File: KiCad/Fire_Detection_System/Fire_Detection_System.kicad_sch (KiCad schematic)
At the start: 12 parts, among them J1 Conn_01x19_Female, J10 Conn_01x01_Pin, J2 Conn_01x19_Female, J3 Conn_01x01_Pin, J4 Conn_01x01_Pin, J5 Conn_01x01_Pin, J6 Conn_01x01_Pin, J7 Conn_01x01_Pin, J8 Conn_01x01_Pin, J9 Conn_01x01_Pin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

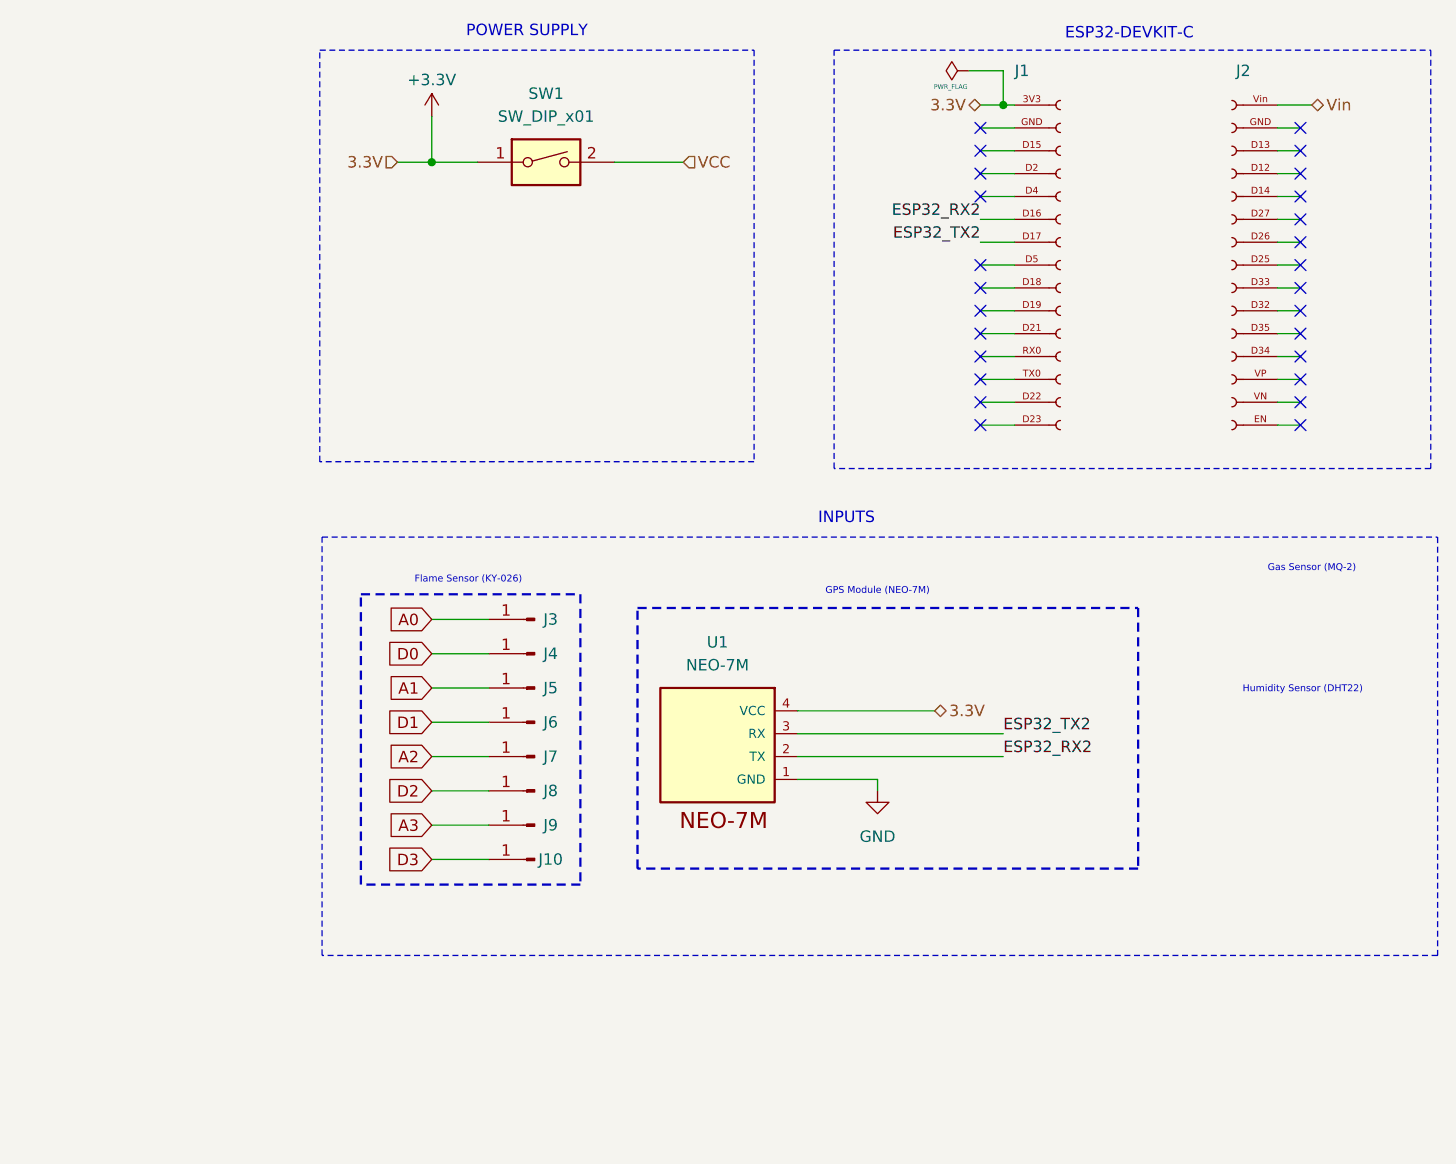
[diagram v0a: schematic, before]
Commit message: feat: Adding Compass Calibration
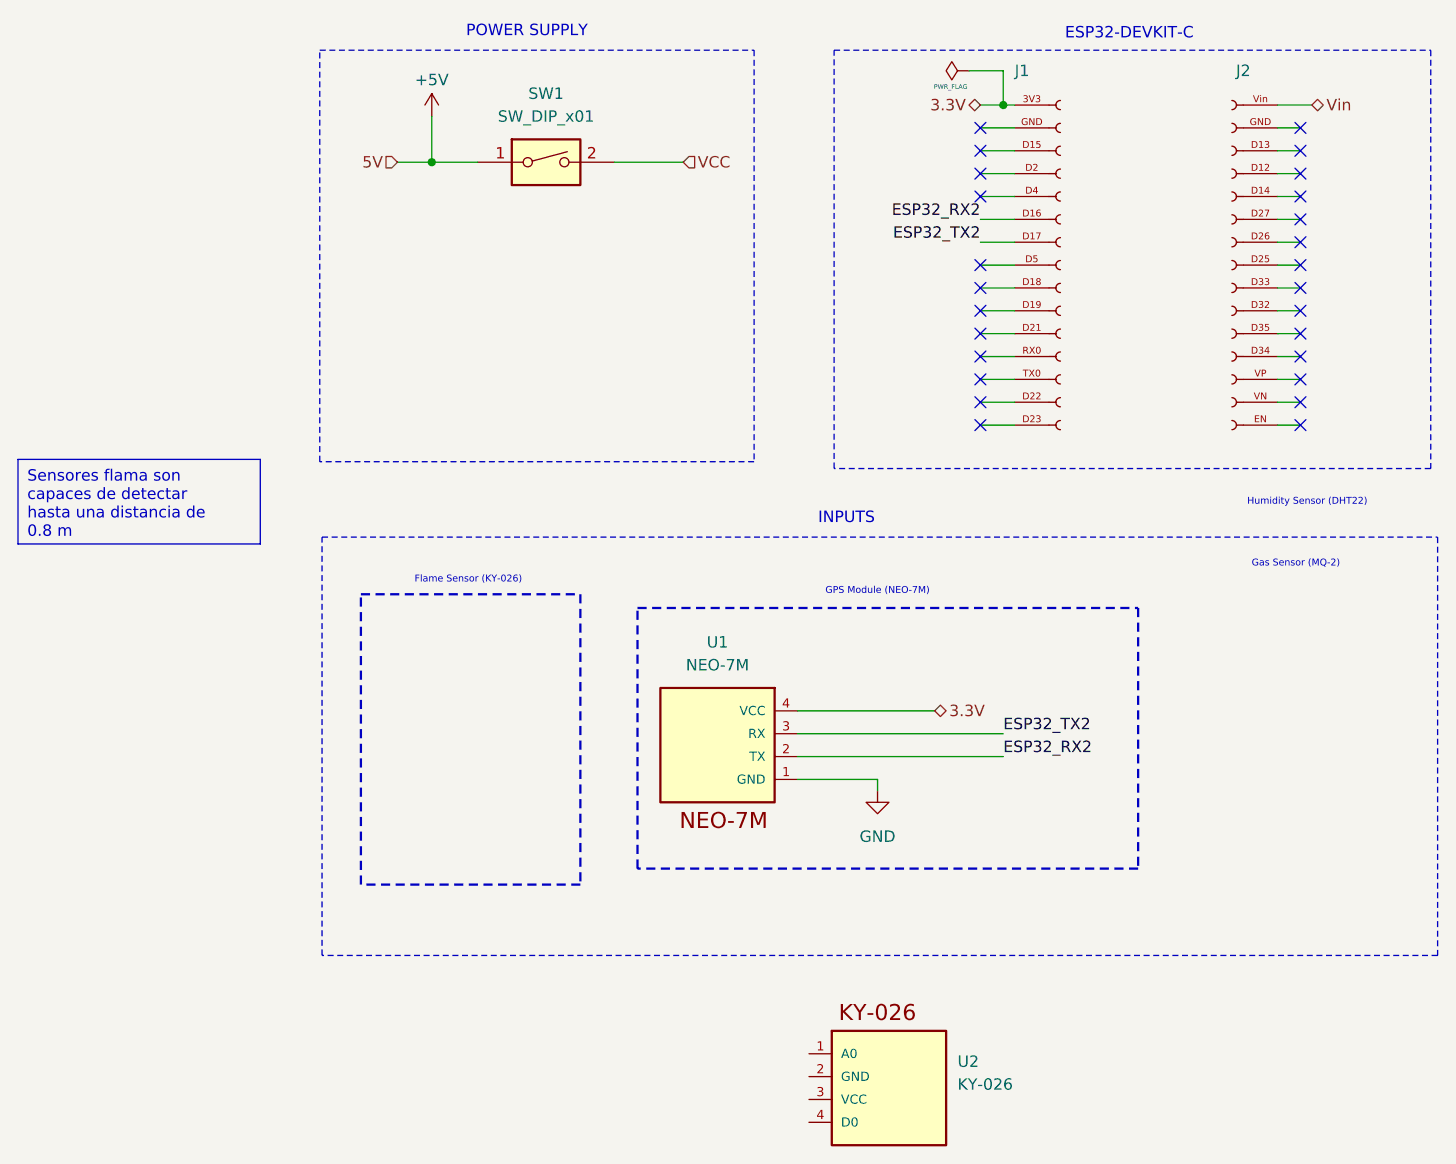
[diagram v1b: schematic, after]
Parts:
- removed J10, J3, J4, J5, J6, J7, J8, J9: Conn_01x01_Pin, Connector_PinHeader_2.54mm:PinHeader_1x01_P2.54mm_Vertical, symbol Connector:Conn_01x01_Pin
- added U2: KY-026, NEO-6M:NEO-6M, symbol KY-026:NEO-6M
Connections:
- net +3.3V renamed 3.3V
- net 3.3V: no longer SW1.1
- new net +5V: SW1.1
